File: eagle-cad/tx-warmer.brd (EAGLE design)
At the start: 44.5 x 44.5 mm, 22 parts

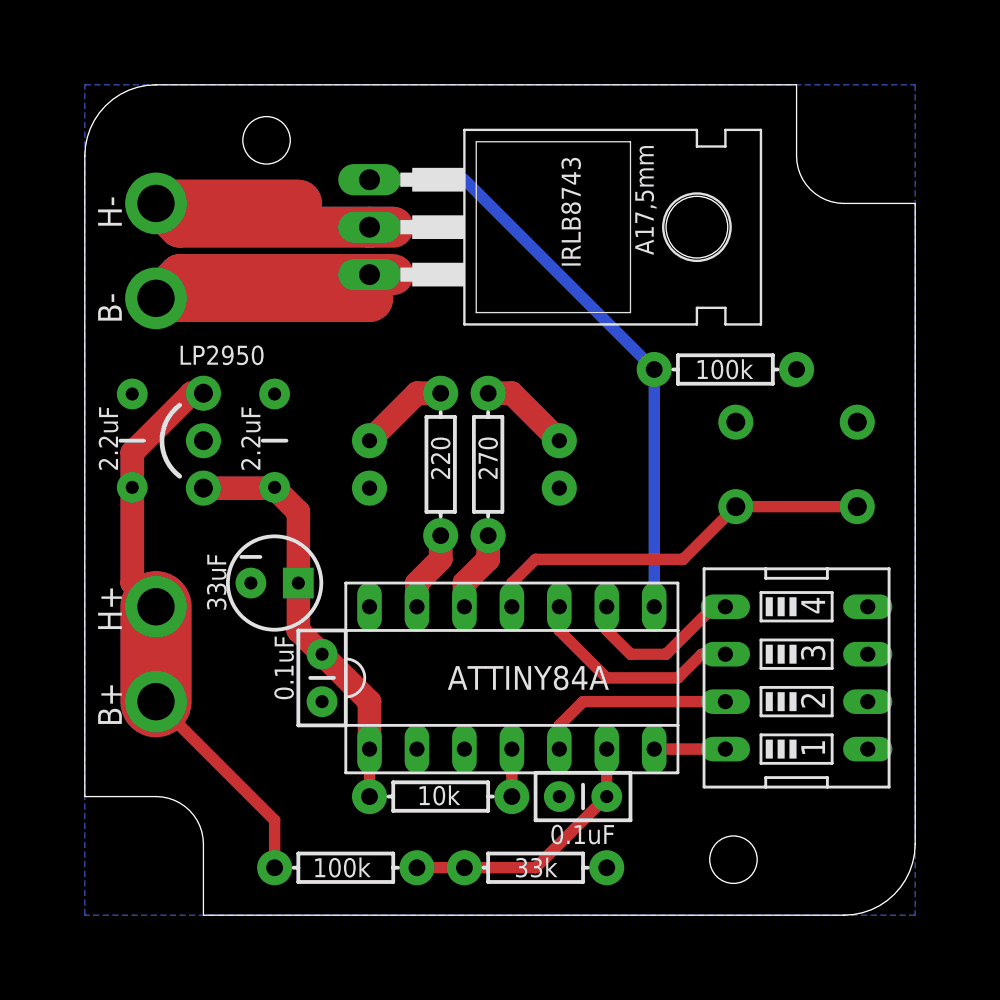
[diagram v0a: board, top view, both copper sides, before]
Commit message: Changed 4P-switch to 6P-switch to utilize all inputs
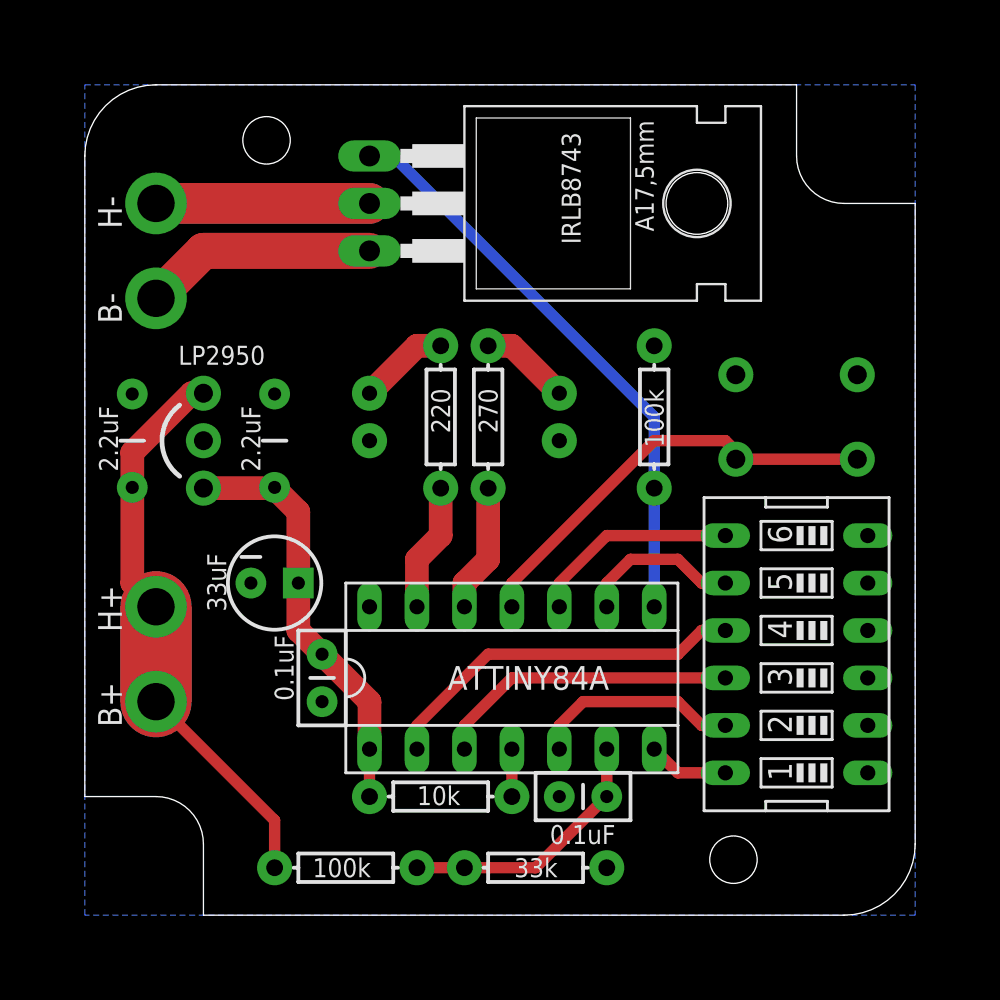
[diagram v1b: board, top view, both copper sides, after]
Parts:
- SW1: device special:EDG-04 -> special:EDG-06
- moved R6 4.58 mm to (29.2, 25.4), turned to 90 degrees
- moved LED1 2.54 mm to (14.0, 25.4)
- moved LED2 2.54 mm to (24.1, 25.4)
- moved R7 2.54 mm to (17.8, 25.4)
- moved R9 2.54 mm to (20.3, 25.4)
- moved SWITCH 2.54 mm to (36.8, 25.4)
- moved SW1 1.27 mm to (36.8, 12.7), turned to 90 degrees
- moved IRLB8743 1.27 mm to (20.3, 36.8)
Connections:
- new net N$21: ATTINY84A.3, SW1.10
- new net N$3: ATTINY84A.2, SW1.9
- net GND: now also SW1.1, SW1.2, SW1.3, SW1.4; no longer SW1.7, SW1.8
- net N$1: now also SW1.12; no longer SW1.4
- net N$2: now also SW1.11; no longer SW1.3
- net N$20: now also ATTINY84A.10, SW1.7; no longer ATTINY84A.9, SW1.1
- net N$5: now also ATTINY84A.9, SW1.8; no longer ATTINY84A.10, SW1.2
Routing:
- net GND: track 49.3 -> 12.5 mm
- net N$3: track 0.00 -> 19.9 mm
- net N$19: track 41.7 -> 22.9 mm
- net N$21: track 0.00 -> 16.3 mm
- net N$5: track 11.7 -> 8.67 mm
- net N$18: track 4.34 -> 6.88 mm
- net N$12: track 4.34 -> 6.88 mm
- net N$13: track 21.5 -> 23.6 mm
- net N$20: track 9.20 -> 11.2 mm
- net N$6: track 32.1 -> 31.2 mm
- net N$1: track 3.81 -> 4.34 mm
- net N$2: track 10.7 -> 11.2 mm
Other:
- board text added: "5"
- board text added: "6"
- board text added: "TX-warmer"
- board text removed: "TX-warmer v1.6"

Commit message: Added GND-plane to top
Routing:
- net GND: track 12.5 -> 0.00 mm
- added copper zone on layer 1, net GND
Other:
- board text added: "TX-warmer r2"
- board text removed: "TX-warmer"
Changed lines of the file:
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@@
 <?xml version="1.0" encoding="utf-8"?>
 <!DOCTYPE eagle SYSTEM "eagle.dtd">
-<eagle version="6.3">
+<eagle version="6.5.0">
 <drawing>
 <settings>
@@
 <hole x="8.4582" y="40.2082" drill="2.54"/>
 <hole x="33.4518" y="1.7018" drill="2.54"/>
-<text x="16.51" y="13.335" size="1.27" layer="22" rot="MR180">TX-warmer</text>
-<text x="12.7" y="10.795" size="1.143" layer="22" rot="MR180">Pertti Erkkilä 2013</text>
+<text x="27.94" y="12.065" size="1.27" layer="22" rot="MR0">TX-warmer r2</text>
+<text x="30.48" y="9.525" size="1.143" layer="22" rot="MR0">Pertti Erkkilä 2013</text>
 <wire x1="3.81" y1="22.225" x2="3.81" y2="26.035" width="0.254" layer="21" curve="-106.260205"/>
 <text x="36.576" y="13.5382" size="1.27" layer="21" rot="R90">4</text>
@@
 <contactref element="C4" pad="2"/>
 <contactref element="C3" pad="2"/>
-<polygon width="0.6096" layer="16" isolate="0.6096">
-<vertex x="-1.27" y="-1.27"/>
-<vertex x="-1.27" y="43.18"/>
-<vertex x="43.18" y="43.18"/>
-<vertex x="43.18" y="-1.27"/>
+<polygon width="0.6096" layer="16" isolate="0.4064">
+<vertex x="-2.54" y="-2.54"/>
+<vertex x="-2.54" y="44.45"/>
+<vertex x="44.45" y="44.45"/>
+<vertex x="44.45" y="-2.54"/>
 </polygon>
 <contactref element="B-" pad="1"/>
@@
 <contactref element="SW1" pad="4"/>
 <contactref element="SW1" pad="5"/>
-<wire x1="13.97" y1="34.29" x2="5.08" y2="34.29" width="1.9304" layer="1"/>
-<wire x1="5.08" y1="34.29" x2="2.54" y2="31.75" width="1.9304" layer="1"/>
+<polygon width="0.6096" layer="1" isolate="0.4064">
+<vertex x="-3.81" y="45.72"/>
+<vertex x="45.72" y="45.72"/>
+<vertex x="45.72" y="-3.81"/>
+<vertex x="-3.81" y="-3.81"/>
+</polygon>
 </signal>
 <signal name="5V">

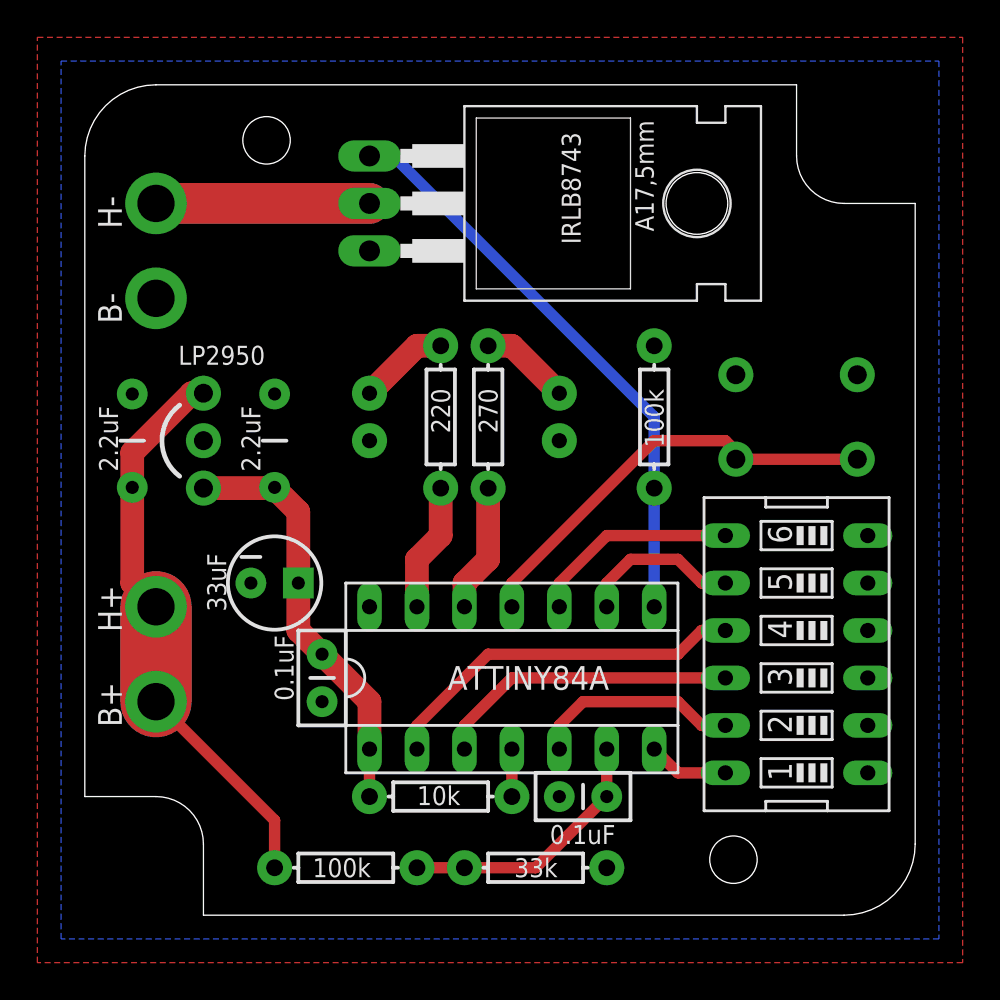
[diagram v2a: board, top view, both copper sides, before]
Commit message: Removed DIP:s, added two sensor ports, bat-pins and prog-interface
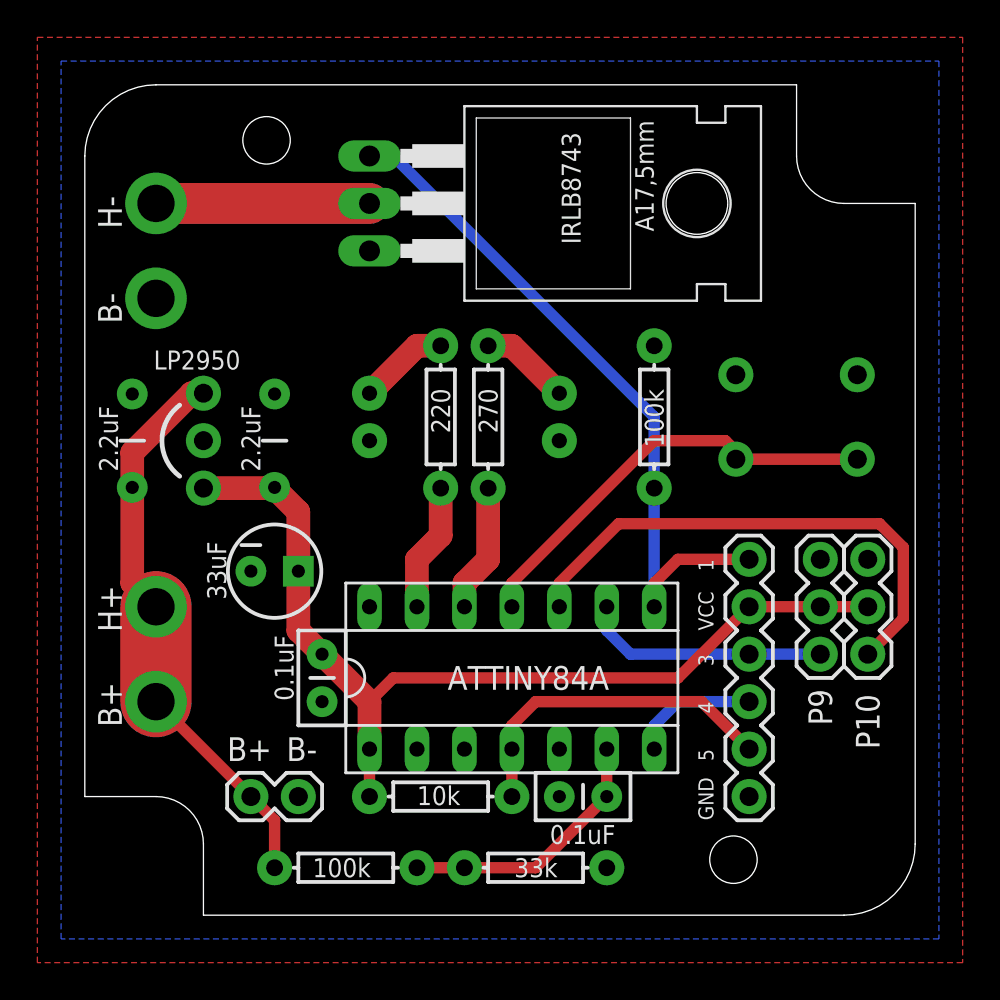
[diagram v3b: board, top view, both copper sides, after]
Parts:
- removed SW1: (no value), special:EDG-06
- added JP1, JP2: (no value), SparkFun-Connectors:1X03
- added JP3: (no value), SparkFun-Connectors:1X06
- added JP4: M02PTH, SparkFun-Connectors:1X02
- moved C5 0.63 mm to (8.89, 17.1)
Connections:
- removed net N$20: ATTINY84A.10, SW1.7
- removed net N$21: ATTINY84A.3, SW1.10
- removed net N$5: ATTINY84A.9, SW1.8
- net 5V: now also JP1.2, JP2.2, JP3.2
- net GND: now also JP1.3, JP2.3, JP3.6, JP4.1; no longer SW1.1, SW1.2, SW1.3, SW1.4, SW1.5, SW1.6
- net N$1: now also ATTINY84A.9, JP2.1, JP3.3; no longer ATTINY84A.7, SW1.12
- net N$11: now also JP3.5
- net N$2: now also ATTINY84A.7, JP3.4; no longer ATTINY84A.5, SW1.11
- net N$3: now also ATTINY84A.10, JP1.1; no longer ATTINY84A.2, SW1.9
- net N$4: now also JP4.2
- net N$6: now also JP3.1
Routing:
- net 5V: track 22.5 -> 51.2 mm
- net N$21: track 16.3 -> 0.00 mm
- net N$11: track 2.54 -> 18.1 mm
- net N$20: track 11.2 -> 0.00 mm
- net N$1: track 4.34 -> 13.2 mm
- net N$5: track 8.67 -> 0.00 mm
- net N$3: track 19.9 -> 28.0 mm
- net N$6: track 31.2 -> 38.1 mm
- net N$2: track 11.2 -> 6.88 mm
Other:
- board text added: "B+"
- board text added: "B-"
- board text added: "GND"
- board text added: "P10"
- board text added: "P9"
- board text added: "VCC"
- board text removed: "2"
- board text removed: "6"

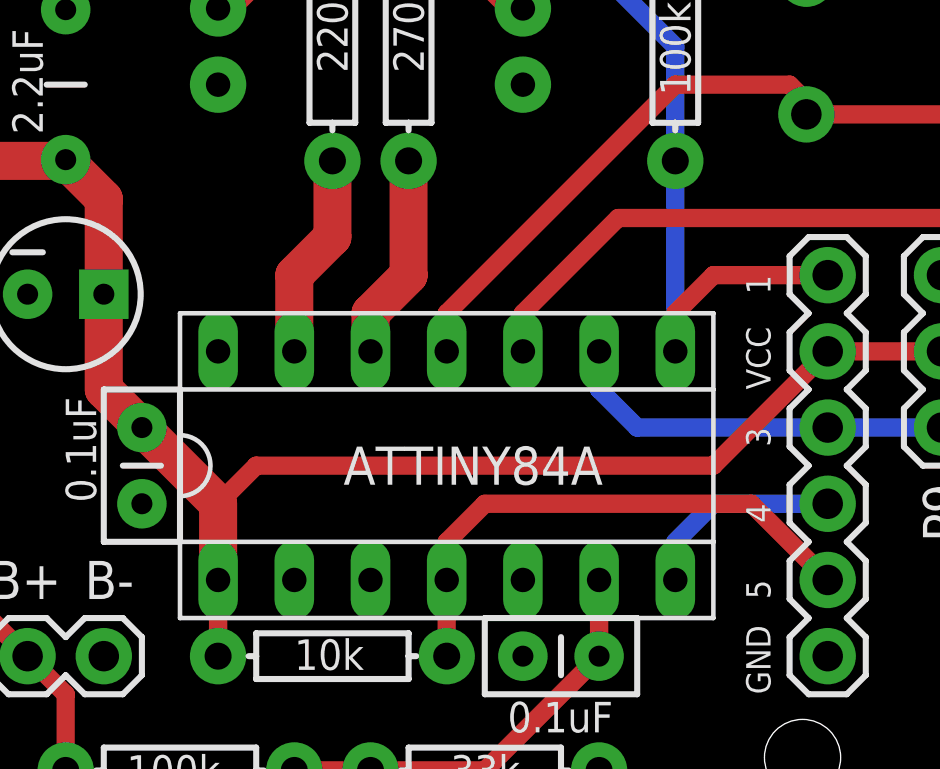
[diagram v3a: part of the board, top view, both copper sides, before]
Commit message: Added SMD-jumpers to empty MC-pins
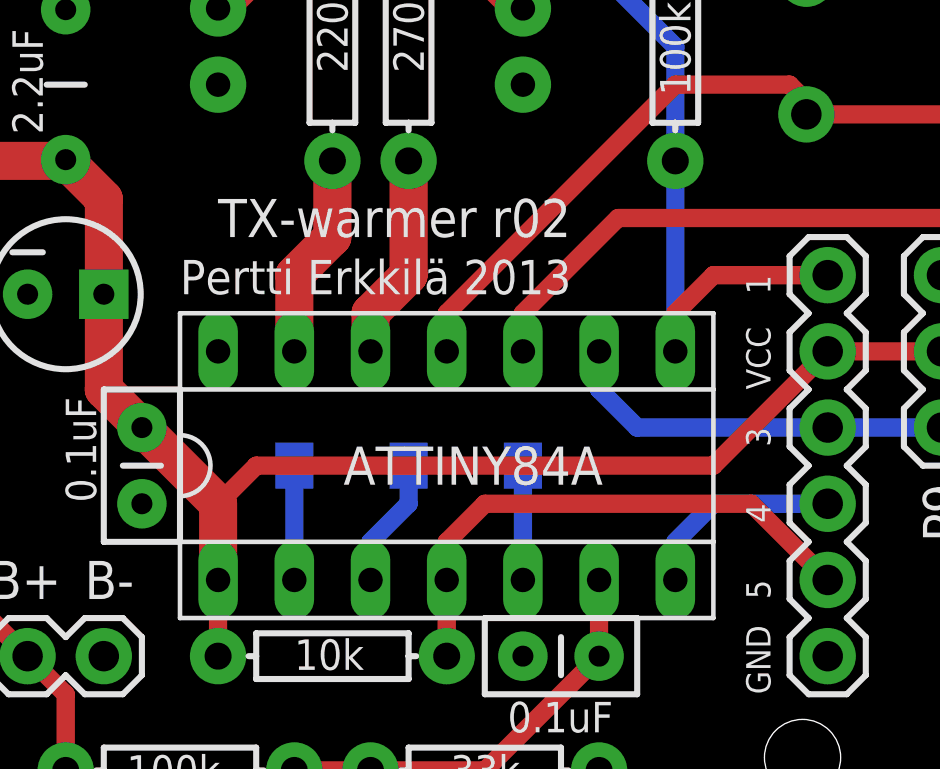
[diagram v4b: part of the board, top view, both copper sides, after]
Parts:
- added JP-1, JP-2, JP-3: (no value), SparkFun-Passives:SJ_2S-NO
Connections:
- new net N$20: ATTINY84A.3, JP-2.1
- new net N$21: ATTINY84A.2, JP-3.1
- new net N$5: ATTINY84A.5, JP-1.1
- net GND: now also JP-1.2, JP-2.2, JP-3.2
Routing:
- net N$20: track 0.00 -> 3.89 mm
- net N$5: track 0.00 -> 3.36 mm
- net N$21: track 0.00 -> 3.36 mm
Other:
- board text added: "TX-warmer r02"
- board text removed: "TX-warmer r2"
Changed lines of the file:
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@@
 <setting verticaltext="up"/>
 </settings>
-<grid distance="0.05" unitdist="inch" unit="inch" style="lines" multiple="1" display="yes" altdistance="0.025" altunitdist="inch" altunit="inch"/>
+<grid distance="0.025" unitdist="inch" unit="inch" style="lines" multiple="1" display="yes" altdistance="0.025" altunitdist="inch" altunit="inch"/>
 <layers>
 <layer number="1" name="Top" color="4" fill="1" visible="yes" active="yes"/>
@@
 <hole x="8.4582" y="40.2082" drill="2.54"/>
 <hole x="33.4518" y="1.7018" drill="2.54"/>
-<text x="27.94" y="12.065" size="1.27" layer="22" rot="MR0">TX-warmer r2</text>
-<text x="30.48" y="9.525" size="1.143" layer="22" rot="MR0">Pertti Erkkilä 2013</text>
+<text x="13.97" y="19.05" size="1.27" layer="21">TX-warmer r02</text>
+<text x="12.7" y="17.145" size="1.143" layer="21">Pertti Erkkilä 2013</text>
 <wire x1="3.81" y1="22.225" x2="3.81" y2="26.035" width="0.254" layer="21" curve="-106.260205"/>
 <text x="32.385" y="3.81" size="0.8128" layer="25" rot="R90">GND</text>
@@
 </element>
 <element name="JP4" library="SparkFun-Connectors" package="1X02" value="M02PTH" x="10.16" y="5.08" smashed="yes" rot="R180"/>
+<element name="JP-1" library="SparkFun-Passives" package="SJ_2S-NO" value="" x="24.13" y="11.43" smashed="yes" rot="MR90">
+<attribute name="NAME" x="25.038" y="12.7" size="0.6096" layer="26" rot="MR0"/>
+<attribute name="VALUE" x="22.479" y="10.522" size="0.4064" layer="28" rot="MR90"/>
+</element>
+<element name="JP-2" library="SparkFun-Passives" package="SJ_2S-NO" value="" x="20.32" y="11.43" smashed="yes" rot="MR90">
+<attribute name="NAME" x="21.228" y="12.7" size="0.6096" layer="26" rot="MR0"/>
+<attribute name="VALUE" x="18.669" y="10.522" size="0.4064" layer="28" rot="MR90"/>
+</element>
+<element name="JP-3" library="SparkFun-Passives" package="SJ_2S-NO" value="" x="16.51" y="11.43" smashed="yes" rot="MR90">
+<attribute name="NAME" x="17.418" y="12.7" size="0.6096" layer="26" rot="MR0"/>
+<attribute name="VALUE" x="14.859" y="10.522" size="0.4064" layer="28" rot="MR90"/>
+</element>
 </elements>
 <signals>
@@
 <contactref element="JP3" pad="6"/>
 <contactref element="JP4" pad="1"/>
+<contactref element="JP-3" pad="2"/>
+<contactref element="JP-2" pad="2"/>
+<contactref element="JP-1" pad="2"/>
 </signal>
 <signal name="5V">
@@
 <wire x1="42.545" y1="18.415" x2="41.275" y2="19.685" width="0.6096" layer="1"/>
 </signal>
+<signal name="N$5">
+<contactref element="ATTINY84A" pad="5"/>
+<contactref element="JP-1" pad="1"/>
+<wire x1="24.13" y1="10.98" x2="24.13" y2="7.62" width="0.6096" layer="16"/>
+</signal>
+<signal name="N$20">
+<contactref element="ATTINY84A" pad="3"/>
+<contactref element="JP-2" pad="1"/>
+<wire x1="19.05" y1="7.62" x2="19.05" y2="8.89" width="0.6096" layer="16"/>
+<wire x1="19.05" y1="8.89" x2="20.32" y2="10.16" width="0.6096" layer="16"/>
+<wire x1="20.32" y1="10.16" x2="20.32" y2="10.98" width="0.6096" layer="16"/>
+</signal>
+<signal name="N$21">
+<contactref element="ATTINY84A" pad="2"/>
+<contactref element="JP-3" pad="1"/>
+<wire x1="16.51" y1="10.98" x2="16.51" y2="7.62" width="0.6096" layer="16"/>
+</signal>
 </signals>
